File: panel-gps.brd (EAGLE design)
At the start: 78.2 x 76.6 mm, 141 parts, among them IC1 MSP430FR698X(1)80-PIN_PN, IC2 MSP430FR698X(1)80-PIN_PN, IC3 FT232RL

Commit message: Little panel tuning
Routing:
- net GND2: vias 37 -> 66
- net GND: vias 40 -> 46

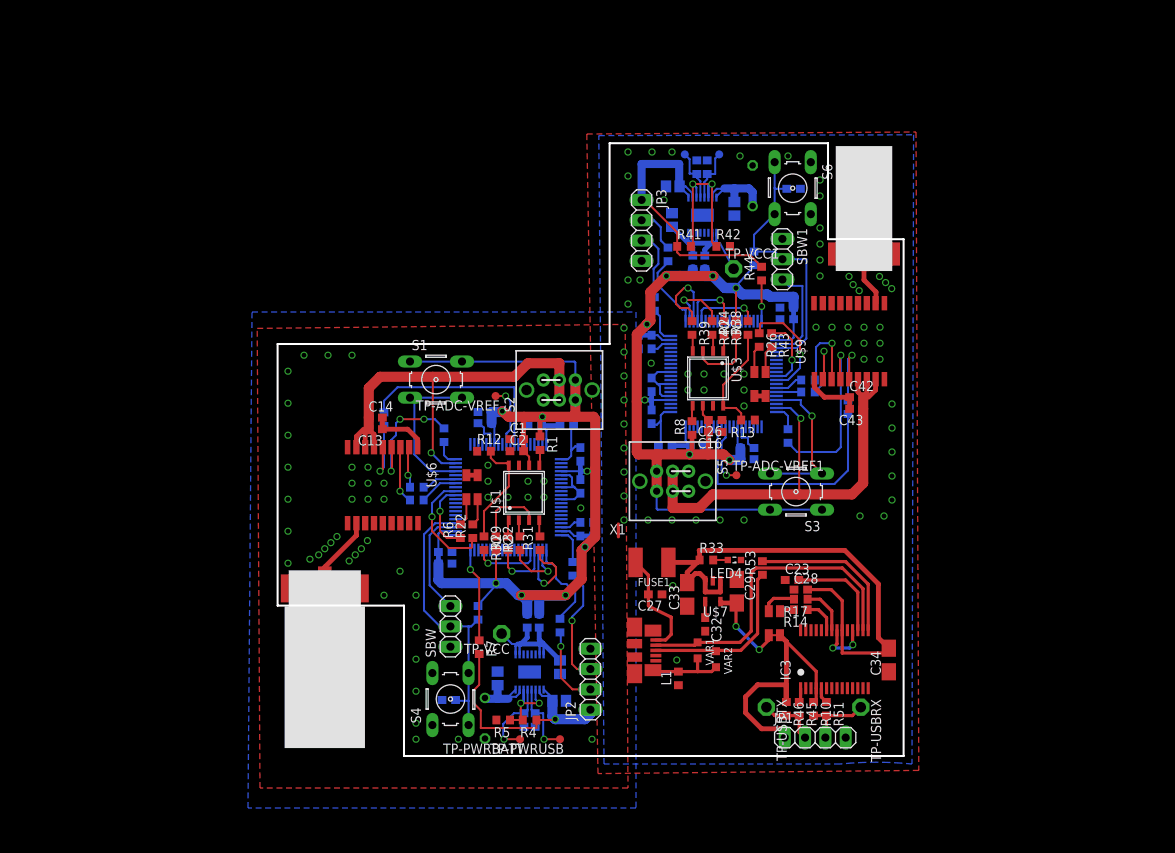
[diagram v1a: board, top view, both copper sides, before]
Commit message: Update panel-gps massively, add holes
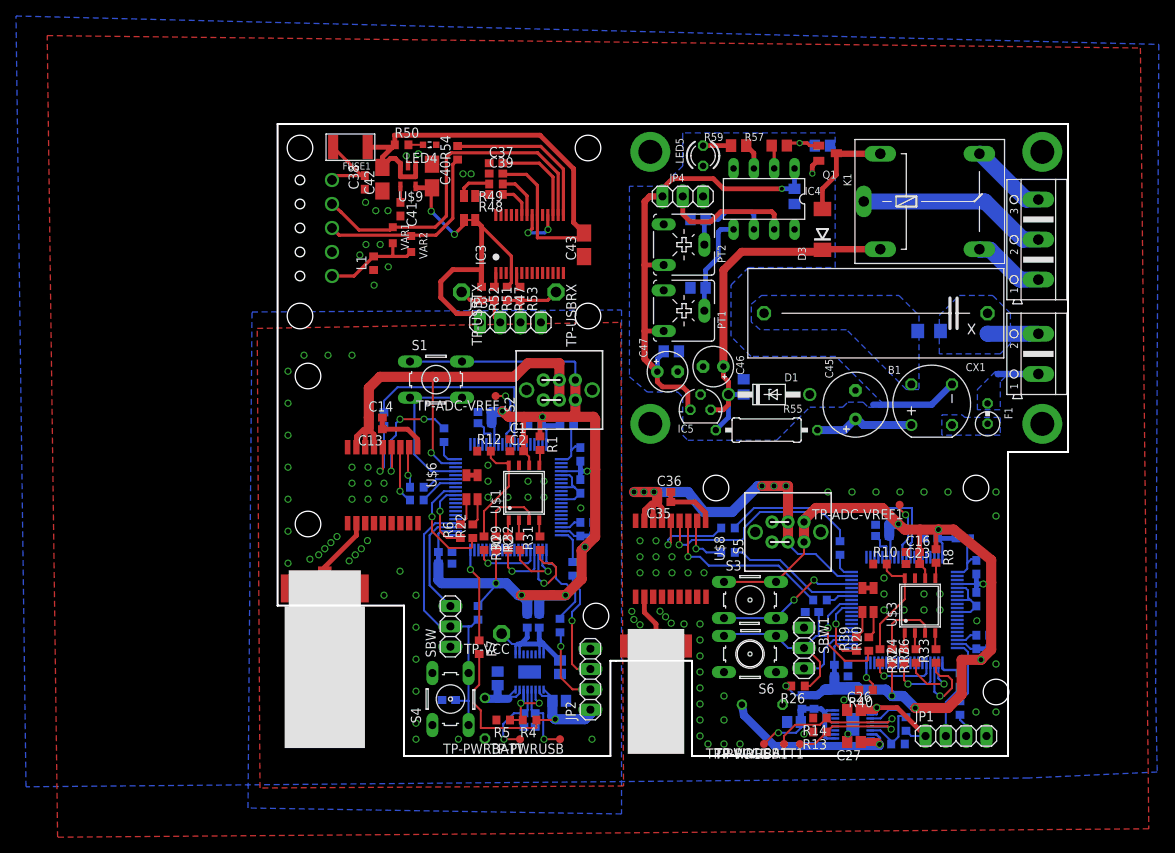
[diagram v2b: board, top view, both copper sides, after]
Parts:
- removed X1: (no value), tagps:USB
- added B1: (no value), rectifier:RB1A
- added C44, C50, C51: 100nF, rcl:C0805
- added C45: 100uF, rcl:E3,5-8
- added C46, C47: (no value), rcl:E2,5-5
- added C48, C49: (no value), rcl:C0805
- added CX1: (no value), rcl:XC27B11
- added D1: BZX85, diode:DO41Z10
- added D3: (no value), diode:DO214AA
- added F1: 3R3, rcl:0309V
- added IC4: PIC12F675P, microchip:DIL8
- added IC5: (no value), v-reg:78LXX
- added JP4: (no value), pinhead:1X03
- added K1: RAS-1215, my_library:RAS-12XX
- added LED5: (no value), led:LED3MM
- added PT1, PT2: (no value), pot:CA6V
- added Q1: BC846, transistor:SOT23
- added R55: 220R, rcl:0309/12
- added R56: 1M, rcl:R1206
- added R57: 2.7k, rcl:R0805
- added R58: 68k, rcl:R0805
- added R59: 150R, rcl:M0805
- added X2: (no value), con-ptr500:AK500/2
- added X3: (no value), con-ptr500:AK500/3
- C23, C28: value 100nF -> 100n
- C26: value 100n -> 4.7uF; device tagps:C0603 -> tagps:C0805
- C27: value 10nF -> 4.7uF at least; device tagps:C0603 -> tagps:C0805
- C29, C33: value 1uF -> 1u; device tagps:A/3216-18W -> tagps:C0603
- C30: value 4.7uF -> 100n; device tagps:C0805 -> tagps:C0603
- C31: value 4.7uF at least -> 1u; device tagps:C0805 -> tagps:C0603
- C32: value 470pF -> 100n
- C34: value 4.7uF -> 100n; device tagps:A/3216-18W -> tagps:C0603
- C37, C39: value 100n -> 100nF
- C38: value 1u -> 10nF
- C40: value 1u -> 1uF; device tagps:C0603 -> tagps:A/3216-18W
- C41: value 100n -> 470pF
- C42: value 100n -> 1uF; device tagps:C0603 -> tagps:A/3216-18W
- C43: value 1u -> 4.7uF; device tagps:C0603 -> tagps:A/3216-18W
- FUSE1: value 500mA -> SMD1206R500SF; device resistor:C1812K -> tagps:F1812
- R10: value 33k -> 470k
- R13: value 470k -> 1k
- R14: value 240 -> 1k
- R17: value 220 -> 470k
- R20: value 1k -> 180
- R21: value 1k -> 100
- R24: value 470k -> 100
- R26: value 180 -> 47k
- R33: value 150 -> 100
- R37: value 47k -> 100k
- R38: value 100 -> 39.2k
- R39: value 100 -> 160
- R41: value 100k -> 0
- R42: value 39.2k -> 0
- R43: value 160 -> 0
- R45, R54: value 100 -> 0
- R46: value 33k -> 100
- R47, R52: value 0 -> 33k
- R48: value 0 -> 240
- R49: value 0 -> 220
- R50: value 100 -> 150
- R53: value 0 -> 100
- TP-VCC1: value TPSQPAD1-13 -> TPSQTP10R; device tagps:P1-13 -> tagps:TP10R
- U$7: value TC1185 -> MWSL1251MWSL1350; device tagps:SOT23-5 -> tagps:MWSL1350
- U$8: value MWSL1251MWSL1350 -> MAX-8C-0; device tagps:MWSL1350 -> tagps:MAX-8
- U$9: value MAX-8C-0 -> TC1185; device tagps:MAX-8 -> tagps:SOT23-5
- moved TP-PWRUSB1 74.7 mm to (63.5, 1.50), flipped to the top, turned to 180 degrees
- moved TP-PWRBATT1 74.4 mm to (65.5, 1.50), flipped to the top, turned to 180 degrees
- moved R51 66.5 mm to (27.3, 57.8)
- moved U$4 66.4 mm to (72.1, 3.95), turned to 0 degrees
- moved C42 65.2 mm to (13.3, 72.1), turned to 90 degrees
- moved G1 64.9 mm to (60.8, 6.42), turned to 180 degrees
- moved C22 64.6 mm to (64.8, 4.25), turned to 0 degrees
- moved IC3 64.4 mm to (31.7, 64.0)
- moved L1 64.4 mm to (12.2, 61.6)
- moved LED3 64.4 mm to (24.2, 68.5)
- moved LED4 64.4 mm to (19.2, 76.4)
- moved TP-USBRX 64.4 mm to (35.0, 58.0)
- moved TP-USBTX 64.4 mm to (23.2, 58.0)
- moved VAR2 64.4 mm to (16.9, 64.0)
- moved VAR1 64.4 mm to (14.6, 65.1)
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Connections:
- removed net N$1 (its old number): IC3.1, R45.1
- removed net N$32 (its old number): C23.2, IC3.17
- new net +12V: C46.+, C50.1, D1.C, D3.C, IC5.IN, K1.1, R55.2
- new net +5V: C44.1, C47.+, C51.1, IC4.1, IC5.OUT, JP4.3, PT1.E, PT2.E
- new net GND1: C16.1, C17.2, C19.1, C20.1, C21.2, C22.2, C23.1, C26.1, C27.2, C28.1, C29.1, C30.1, C31.1, C32.2, C33.2, C34.2, C35.1, C36.2, C37.1, C38.1, C39.1, C40.-, C41.2, C42.-, C43.-, G1.-, IC2.21, IC2.46, IC2.6, IC2.61, IC2.65, IC2.68, IC2.71, IC2.78, IC3.18, IC3.21, IC3.25, IC3.26, IC3.7, JP1.4, JP3.4, L1.1, LED2.1, LED2.3, LED4.C, R10.1, R13.2, R14.2, R38.2, S5.1.1, S5.1.2, S6.1, S6.2, SBW1.1, U$3.7, U$4.EXP, U$7.P$1, U$7.P$3, U$8.1, U$8.10, U$8.12, U$9.2
- new net LED: IC4.3, R59.2
- new net N$30: R37.2, R38.1, U$4.3, U$4.6
- new net N$43: LED2.4, R39.2
- new net N$68: D3.A, K1.2, Q1.3
- new net N$69: B1.+, C45.+, R55.1
- new net N$70: K1.P, X3.2
- new net N$71: K1.S, X3.1
- new net N$72: K1.O, X3.3
- new net N$73: B1.AC1, CX1.2, R56.2
- new net N$74: B1.AC2, F1.1
- new net N$75: CX1.1, R56.1, X2.2
- new net N$76: Q1.1, R57.2, R58.2
- new net N$77: LED5.A, R59.1
- new net N$81: F1.2, X2.1
- new net PT1: C48.1, IC4.6, PT2.S
- new net PT2: C49.1, IC4.5, PT1.S
- new net RL1: IC4.2, R57.1
- new net THERM: IC4.7, JP4.2
- net ADC-BATT2: now also R13.1; no longer R20.1
- net FT232-RX: now also JP3.3, R47.2, R53.2; no longer JP1.3, R10.2, R51.2
- net FT232-TX: now also JP3.2, R51.2, R52.2; no longer JP1.2, R45.2, R46.2
- net GND2: now also B1.-, C44.2, C45.-, C46.-, C47.-, C48.2, C49.2, C50.2, C51.2, D1.A, IC4.8, IC5.GND, JP4.1, LED5.K, PT1.A, PT2.A, Q1.2, R58.1; no longer C16.1, C17.2, C19.1, C20.1, C21.2, C22.2, C23.1, C26.1, C27.1, C28.1, C29.-, C30.1, C31.2, C32.2, C33.-, C34.-, C35.1, C36.1, C37.1, C38.1, C39.2, C40.2, C41.2, C42.1, C43.2, G1.-, IC2.21, IC2.46, IC2.6, IC2.61, IC2.65, IC2.68, IC2.71, IC2.78, IC3.18, IC3.21, IC3.25, IC3.26, IC3.7, JP1.4, JP3.4, L1.1, LED2.1, LED2.3, LED4.C, R13.1, R20.2, R21.2, R42.2, S5.1.1, S5.1.2, S6.1, S6.2, SBW1.1, U$3.7, U$4.EXP, U$7.2, U$8.P$1, U$8.P$3, U$9.1, U$9.10, U$9.12, X1.5
- net LED5: now also R39.1; no longer R43.1
- net LED6: now also R20.1; no longer R26.1
- net MB-GPS-RX2: now also R21.2, U$8.3; no longer R27.2, U$9.3
- net MB-GPS-TIMEPULSE2: now also R42.1; no longer R48.1
- net MB-GPS-TX2: now also R46.2, U$8.2; no longer R54.2, U$9.2
- net MB-GPS-WAKEUP2: now also R41.1; no longer R47.1
- net MB-PWR_GPS_SENSE2: now also C35.2, C36.1, U$8.6, U$8.7, U$8.8; no longer C42.2, C43.1, U$9.6, U$9.7, U$9.8
- net MCU-RX-FT2: now also R44.2; no longer R50.2
- net MCU-TX-FT2: now also JP1.3; no longer JP3.3
- net N$31: now also R17.1, U$3.3; no longer R41.2, R42.1, U$4.3, U$4.6
- net N$37: now also TP-PWRUSB1.TP, U$4.4; no longer IC3.23
- net N$38: now also C22.1, R43.1, R45.1, TP-VCC1.TP, U$4.10, U$4.15, U$4.16, U$4.9; no longer IC3.22, R17.1
- net N$39: now also IC2.3, R33.1; no longer LED3.1, R14.2
- net N$40: now also IC2.4, R24.1; no longer R53.1, VAR2.1, X1.3
- net N$41: now also R10.2, R27.1, U$3.8; no longer IC3.16, VAR1.1, X1.2
- net N$42: now also IC2.2, R36.1; no longer R24.1, U$3.3
- net N$44: now also LED2.2, R20.2; no longer R21.1, TP-PWRUSB1.TP, U$4.4
- net N$48: now also IC2.34, R21.1; no longer C22.1, R49.1, R52.1, TP-VCC1.TP, U$4.10, U$4.15, U$4.16, U$4.9
- net N$49: now also R41.2, U$8.5; no longer C32.1, U$7.4
- net N$50: now also R42.2, U$8.4; no longer IC2.3, R39.1
- net N$51: now also U$7.P$2, U$8.11; no longer IC2.4, R36.1
- net N$52: now also JP1.2, R44.1; no longer R13.2, R38.1, U$3.8
- net N$53: now also IC2.35, R46.1; no longer C27.2, FUSE1.2, X1.1
- net N$54: now also IC3.1, R51.1; no longer L1.2, VAR1.2, VAR2.2, X1.6
- net N$55: now also C37.2, IC3.17; no longer IC2.2, R40.1
- net N$56: now also IC3.23, R48.1; no longer LED2.4, R43.2
- net N$57: now also IC3.22, R49.1; no longer LED2.2, R26.2
- net N$58: now also LED3.1, R48.2; no longer LED3.3, R17.2
- net N$59: now also R54.1, VAR2.1; no longer IC2.34, R27.1
- net N$60: now also IC3.16, VAR1.1; no longer LED4.A, R33.2
- net N$61: now also C41.1, U$9.4; no longer R47.2, U$9.5
- net N$62: now also C38.2, FUSE1.2; no longer R48.2, U$9.4
- net N$63: now also L1.2, VAR1.2, VAR2.2; no longer U$8.P$2, U$9.11
- net N$64: now also LED3.3, R49.2; no longer JP3.2, R50.1
- net N$65: now also LED4.A, R50.2; no longer IC3.5, R51.1
- net N$66: now also IC3.5, R53.1; no longer IC3.15, R53.2
- net N$67: now also IC3.15, R54.2; no longer IC2.35, R54.1
- net PWR-USB-SENSE2: now also R40.1; no longer R44.1
- net SBW-TDO/TDI2: now also R26.1; no longer R37.1
- net SPICLK2: now also R36.2; no longer R40.2
- net SPICSN2: now also R33.2; no longer R39.2
- net SPISI2: now also R24.2; no longer R36.2
- net SPISO2: now also R27.2; no longer R38.2
- net VBUS: now also C39.2, C42.+, C43.+, R50.1, U$9.1, U$9.3; no longer C28.2, C33.+, C34.+, R33.1, U$7.1, U$7.3
- net VCC1: now also C23.2, C28.2, C29.2, C30.2, C31.2, C32.1, C33.1, C34.1, R17.2, R26.2, R43.2, R45.2; no longer C26.2, C35.2, C36.2, C37.2, C38.2, C39.1, C40.1, C41.1, R24.2, R37.2, R49.2, R52.2
- net VCCUSB: now also C40.+, JP3.1, R47.1, R52.1, U$9.5; no longer C29.+, JP1.1, R10.1, R46.1, U$7.5
- net VCCUSBGPS2: now also C26.2, JP1.1, R37.1, R40.2; no longer C30.2, JP3.1, R41.1, R44.2
- net VCC_BATT_IN2: now also C27.1; no longer C31.1
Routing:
- net +5V: track 0.00 -> 61.1 mm, vias 0 -> 1
- net +12V: track 0.00 -> 47.3 mm
- net N$60: track 1.83 -> 44.1 mm, vias 0 -> 1
- net GND1: track 0.00 -> 37.4 mm, vias 0 -> 68
- net N$41: track 40.4 -> 13.8 mm
- net GND2: track 39.2 -> 12.9 mm, vias 66 -> 1
- net N$70: track 0.00 -> 23.8 mm
- net N$59: track 3.51 -> 24.1 mm, vias 0 -> 1
- net VCCUSBGPS2: track 36.3 -> 17.7 mm, vias 0 -> 1
- net N$66: track 20.2 -> 1.90 mm
- net N$48: track 21.0 -> 3.31 mm
- net THERM: track 0.00 -> 17.2 mm
- net N$67: track 3.10 -> 20.2 mm
- net N$50: track 11.0 -> 27.9 mm
- net VCC_BATT_IN2: track 10.9 -> 26.7 mm, vias 0 -> 1
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- added copper zone on layer 1, net GND1
- added copper zone on layer 16, net GND1
- added copper zone on layer 16, net N$73
- added copper zone on layer 16, net N$74
- added copper zone on layer 16, net N$75
- added copper zone on layer 16, net N$81
- removed copper zone on layer 1, net GND2
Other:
- board size 78.2 x 76.6 mm -> 98.8 x 79 mm
- board text added: "B1"
- board text added: "C1"
- board text added: "C3"
- board text added: "C4"
- board text added: "C5"
- board text added: "C6"
- board text added: "C7"
- board text added: "C8"
- board text added: "C9"
- board text added: "CX1"
- board text added: "D1"
- board text added: "D3"
- board text added: "F1"
- board text added: "GND-DP-DM-VCC"
- board text added: "GND-RST-TST"
- board text added: "GPS: OFF - ON"
- board text added: "IC1"
- board text added: "IC2"
- board text added: "JP2"
- board text added: "K1"
- board text added: "LED1"
- board text added: "PT1"
- board text added: "PT2"
- board text added: "Q1"
- board text added: "R1"
- board text added: "R2"
- board text added: "R3"
- board text added: "R5"
- board text added: "R7"
- board text added: "SHLD"
- board text added: "TIMER v4"
- board text removed: "GPS: ON - OFF"
- board text removed: "taGPS v0.3"
